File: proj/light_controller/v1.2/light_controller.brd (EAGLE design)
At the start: 152.4 x 152.4 mm, 129 parts, among them J1 0022232051, J2 OPENAG-I2C-RJ12, J3 OPENAG-I2C-RJ12, J4 1377G2, J5 OPENAG-RS485-RJ12, J6 OPENAG-RS485-RJ12, J7 OPENAG-I2C-HEADER, J8 JUMPER, SW1 BF3-1020, U1 RCD-24-0.70/VREF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

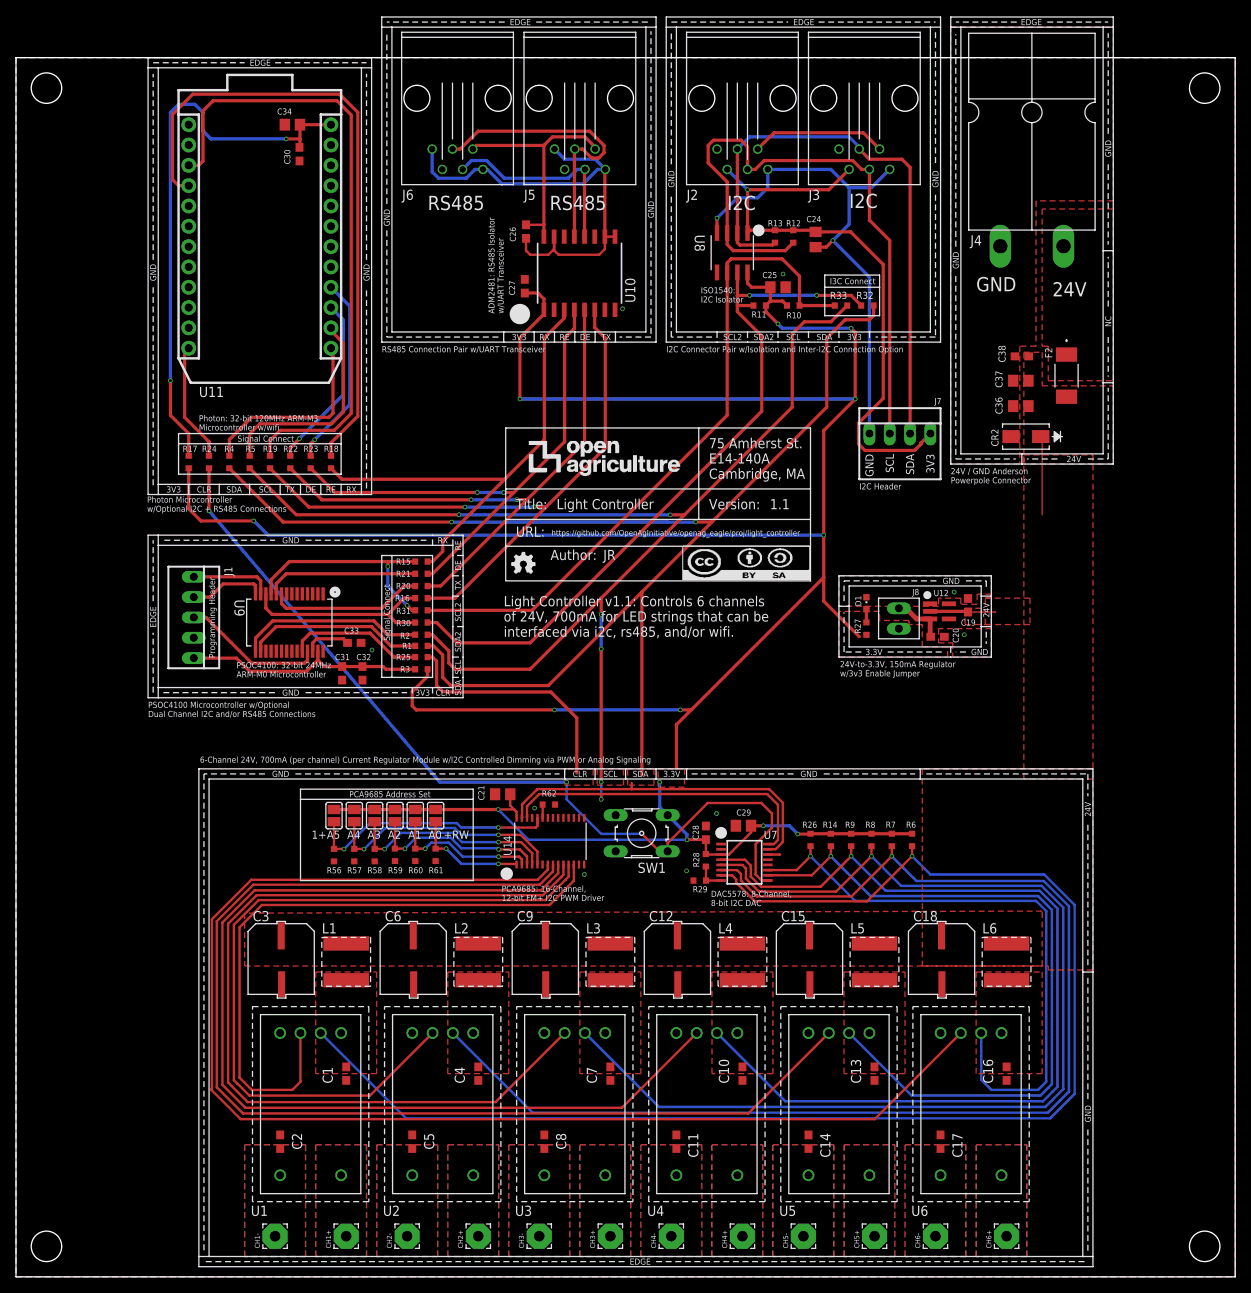
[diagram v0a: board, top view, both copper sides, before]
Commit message: create v1.2 of light controller
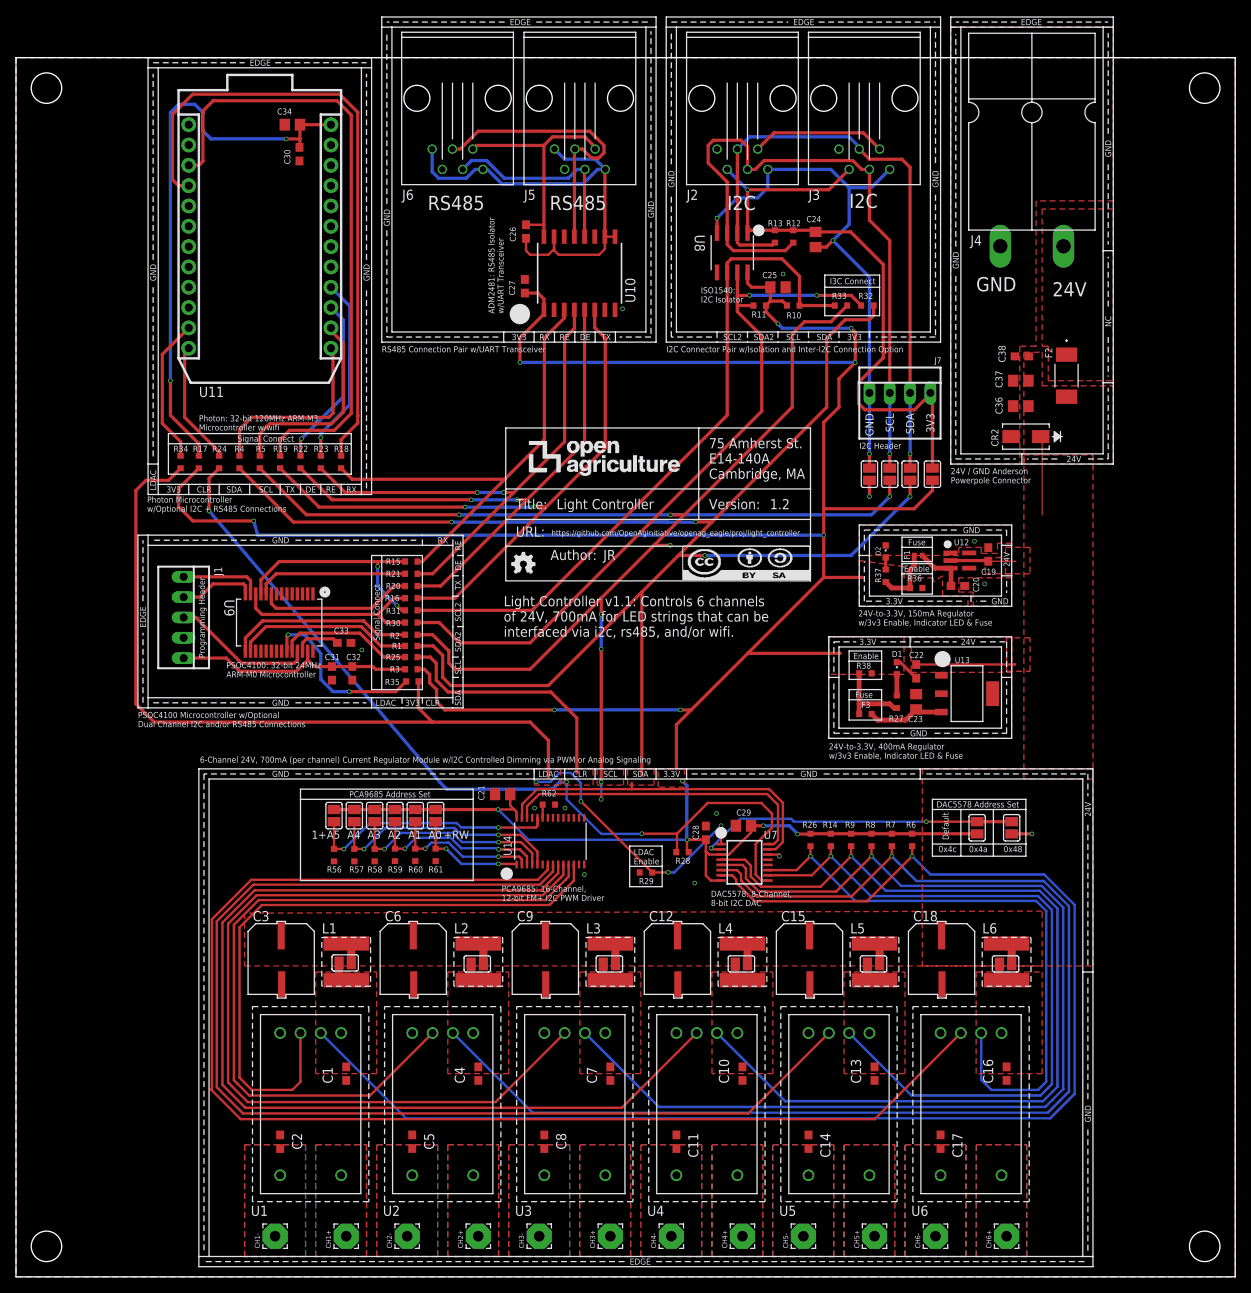
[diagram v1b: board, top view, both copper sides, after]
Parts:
- removed J8: JUMPER, openag-connectors:1X2-100-MIL-HEADER
- removed SW1: BF3-1020, openag-switches:B3F-10XX
- added C22: 0.1uF, openag-capacitors:C0603
- added C23: 10uF, openag-capacitors:C0805
- added D2: APT1608CGCK, openag-diodes:CHIPLED_0603
- added F1: F0402G0R15FNTR, openag-fuses:0402
- added F3: 0448.400MR, openag-fuses:0603
- added R34, R35, R36, R38: 0 OHM, openag-resistors:RC0603N
- added R37: 100 OHM, openag-resistors:RC0603N
- added SJ_A10, SJ_A11, SJ_A12, SJ_A13, SJ_A14, SJ_A15, SJ_A16, SJ_A17, SJ_A6, SJ_A7, SJ_A8, SJ_A9: (no value), openag-connectors:SOLDERJUMPER_REFLOW_NOPASTE
- added U13: LM2937IMP3.3NOPB, openag-regulators:MP04A
- R29: value 3.9K -> 0 OHM
- moved R27 9.91 mm to (110.1, 71.9)
- moved D1 8.98 mm to (110.1, 76.1)
- moved C19 6.84 mm to (121.5, 90.3)
- moved C20 6.84 mm to (117.7, 86.4)
- moved U12 6.84 mm to (118.0, 89.5)
- moved R29 6.81 mm to (78.7, 50.5)
- moved J7 5.08 mm to (110.5, 110.5)
- moved R28 3.09 mm to (83.3, 53.1), turned to 180 degrees
- moved C31 1.27 mm to (39.5, 75.4)
- moved C32 1.27 mm to (42.0, 75.4)
- moved J1 1.27 mm to (21.0, 82.4)
- moved R1 1.27 mm to (49.4, 78.9)
- moved R15 1.27 mm to (49.4, 89.4)
- moved R16 1.27 mm to (49.4, 84.8)
- moved R18 1.27 mm to (40.6, 101.9)
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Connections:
- removed net 2.6V: R28.1, R29.2, U7.8
- removed net REG_3V3: C20.1, J8.1, U12.3
- new net !LDAC!: R29.2, R34.2, R35.2, U7.1
- new net ADDR0: SJ_A16.2, SJ_A17.2, U7.2
- new net N$10: C23.1, F3.1, U13.3
- new net N$12: D2.A, R37.1
- new net N$9: C20.1, F1.1, U12.3
- new net P0[6]: R35.1, U9.23
- new net PHOTON_A1: R34.1, U11.11
- new net REG_3V3_150MA: F1.2, R36.1, R37.2
- new net REG_3V3_400MA: F3.2, R27.2, R38.1
- new net TAB: U13.4
- net +24V: now also C22.1, SJ_A10.2, SJ_A11.2, SJ_A6.2, SJ_A7.2, SJ_A8.2, SJ_A9.2, U13.1
- net +3V3: now also R28.1, R36.2, R38.2, SJ_A15.1, SJ_A16.1, U7.8; no longer J8.2, R27.2, R28.2, SW1.3
- net DAC_!CLR!: now also R28.2; no longer SW1.1
- net GND: now also C22.2, C23.2, D2.C, SJ_A12.1, SJ_A17.1, U13.2; no longer U7.1
- net I2C_3V3: now also SJ_A15.2
- net I2C_GND: now also SJ_A12.2
- net N$1: now also SJ_A6.1
- net N$2: now also SJ_A7.1
- net N$4: now also SJ_A8.1
- net N$5: now also SJ_A9.1
- net N$6: now also SJ_A10.1
- net N$7: now also SJ_A11.1
- net SCL: now also SJ_A13.1
- net SCL1: now also SJ_A13.2
- net SDA: now also SJ_A14.1
- net SDA1: now also SJ_A14.2
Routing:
- net !LDAC!: track 0.00 -> 132.0 mm, vias 0 -> 4
- net ADDR0: track 0.00 -> 40.7 mm, vias 0 -> 2
- net SDA: track 214.6 -> 248.6 mm, vias 2 -> 4
- net +3V3: track 372.0 -> 404.5 mm
- net SCL: track 201.8 -> 234.2 mm, vias 6 -> 8
- net +24V: track 18.3 -> 45.8 mm
- net P0[6]: track 0.00 -> 22.3 mm, vias 0 -> 2
- net PHOTON_A1: track 0.00 -> 18.3 mm
- net N$10: track 0.00 -> 10.1 mm
- net REG_3V3_400MA: track 0.00 -> 10.0 mm
- net GND: track 1.72 -> 9.52 mm, vias 9 -> 13
- net REG_3V3_150MA: track 0.00 -> 7.65 mm
- net REG_3V3: track 6.71 -> 0.00 mm
- net N$9: track 0.00 -> 6.45 mm
- net SDA1: track 73.9 -> 78.2 mm, vias 0 -> 1
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- added copper zone on layer 1, net !LDAC!
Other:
- board text added: "0x48"
- board text added: "0x4a"
- board text added: "0x4c"
- board text added: "24V-to-3.3V, 150mA Regulator w/3v3 Enable, Indicator LED & Fuse"
- board text added: "24V-to-3.3V, 400mA Regulator w/3v3 Enable, Indicator LED & Fuse"
- board text added: "DAC5578 Address Set"
- board text added: "Default"
- board text added: "Enable"
- board text added: "Fuse"
- board text added: "LDAC"
- board text added: "LDAC Enable"
- board text removed: "24V-to-3.3V, 150mA Regulator w/3v3 Enable Jumper"

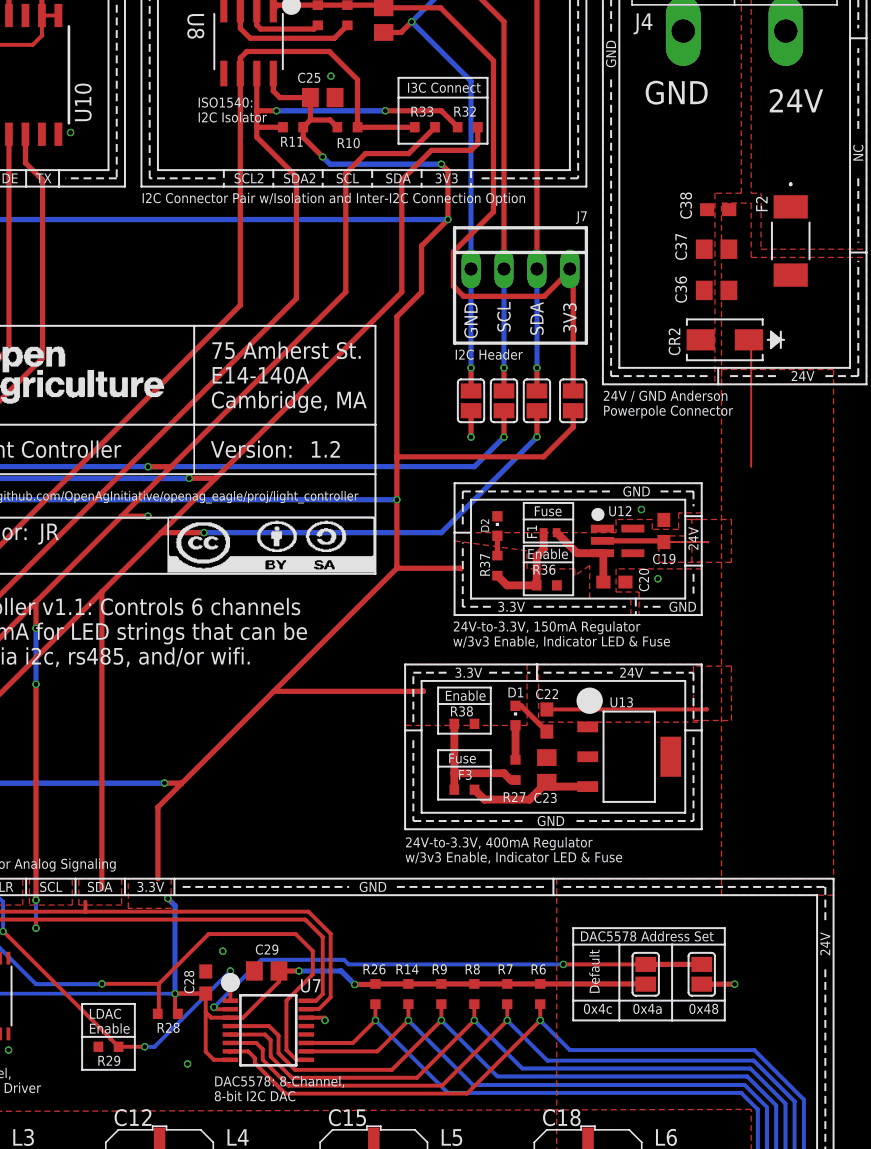
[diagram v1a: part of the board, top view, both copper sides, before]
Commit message: minor silkscreen changes to light controller v1.2
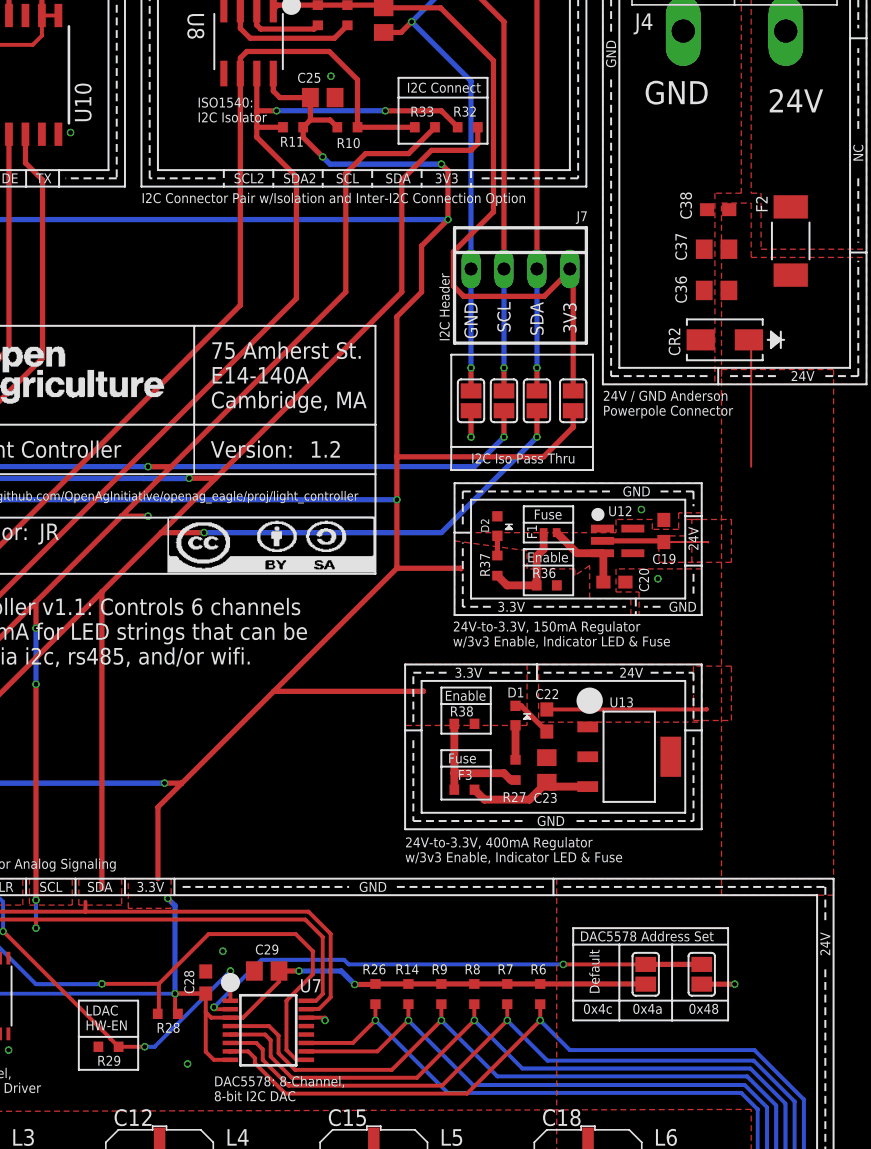
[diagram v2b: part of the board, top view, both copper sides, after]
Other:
- board text added: "I2C Connect"
- board text added: "I2C Iso Pass Thru"
- board text added: "LDAC HW-EN"
- board text removed: "I3C Connect"
- board text removed: "LDAC Enable"

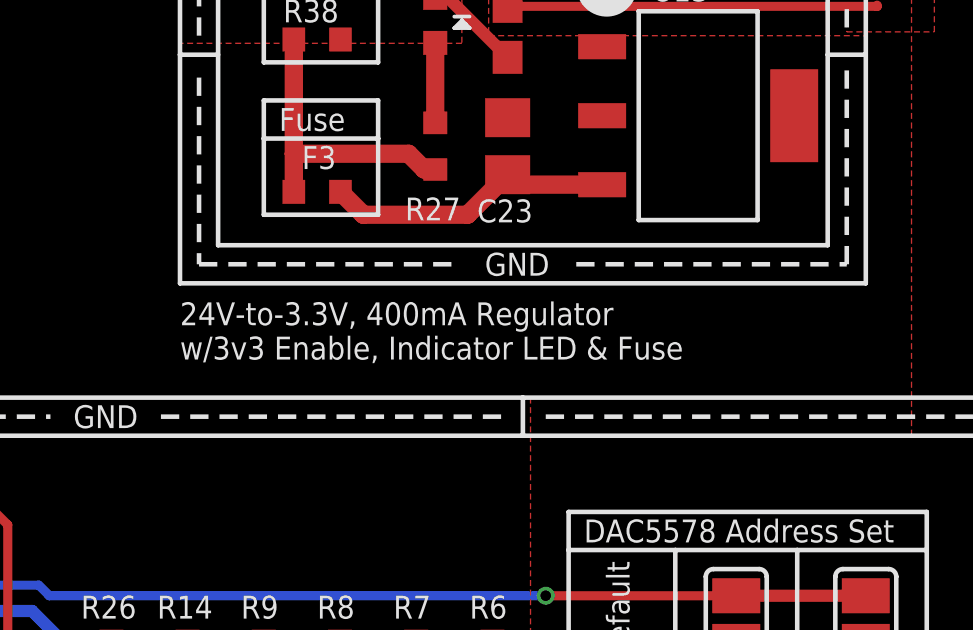
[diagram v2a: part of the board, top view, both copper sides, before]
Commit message: cleaned up design blocks, added co2 sensor node v2.0
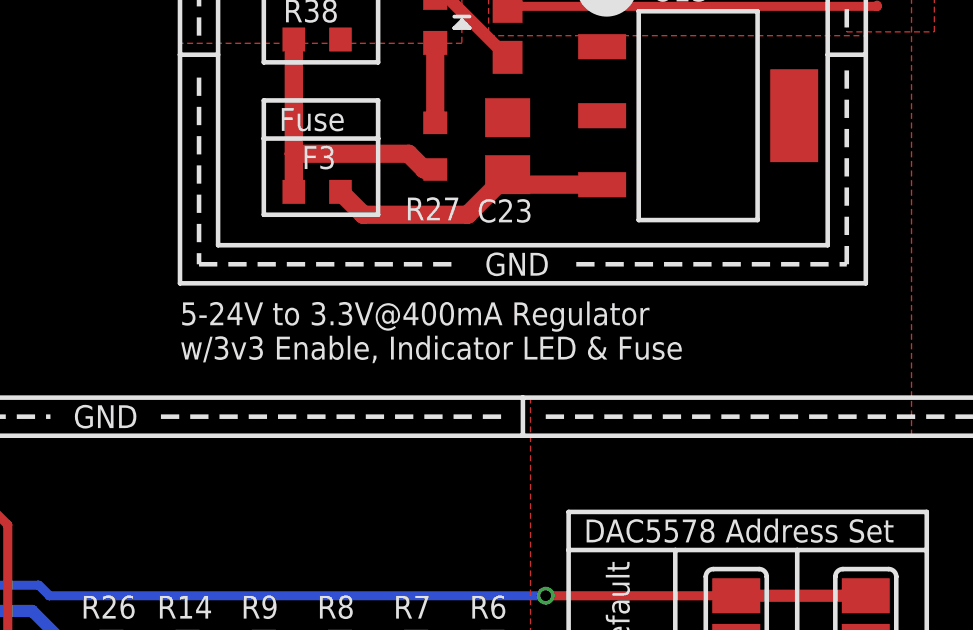
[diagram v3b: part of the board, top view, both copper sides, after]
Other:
- board text added: "5-24V to 3.3V@400mA Regulator w/3v3 Enable, Indicator LED & Fuse"
- board text removed: "24V-to-3.3V, 400mA Regulator w/3v3 Enable, Indicator LED & Fuse"
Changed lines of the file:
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@@
 <setting verticaltext="up"/>
 </settings>
-<grid distance="10" unitdist="mil" unit="mil" style="lines" multiple="1" display="yes" altdistance="1" altunitdist="mil" altunit="mil"/>
+<grid distance="50" unitdist="mil" unit="mil" style="lines" multiple="1" display="yes" altdistance="5" altunitdist="mil" altunit="mil"/>
 <layers>
 <layer number="1" name="Top" color="4" fill="1" visible="yes" active="yes"/>
@@
 <wire x1="120.523" y1="79.375" x2="123.825" y2="79.375" width="0.1524" layer="21" style="shortdash"/>
 <wire x1="123.825" y1="79.375" x2="123.825" y2="75.565" width="0.1524" layer="21" style="shortdash"/>
-<text x="101.6" y="64.77" size="0.762" layer="21">24V-to-3.3V, 400mA Regulator
+<text x="101.6" y="64.77" size="0.762" layer="21">5-24V to 3.3V@400mA Regulator
 w/3v3 Enable, Indicator LED &amp; Fuse</text>
 <wire x1="110.744" y1="89.408" x2="114.554" y2="89.408" width="0.1524" layer="21"/>
@@
 <attribute name="NAME" x="24.765" y="88.773" size="1.016" layer="25" ratio="10" rot="R270"/>
 <attribute name="POPULATE" value="YES" x="20.955" y="82.423" size="1.778" layer="27" rot="R270" display="off"/>
+<attribute name="VALUE" x="19.177" y="79.121" size="1.016" layer="27" ratio="10" rot="R90"/>
 <attribute name="VALUE" value="0022232051" x="20.955" y="82.423" size="1.778" layer="27" rot="R270" display="off"/>
-<attribute name="VALUE" x="19.177" y="79.121" size="1.016" layer="27" ratio="10" rot="R90"/>
 <attribute name="VERIFIED" value="NO" x="20.955" y="82.423" size="1.778" layer="27" rot="R270" display="off"/>
 </element>
